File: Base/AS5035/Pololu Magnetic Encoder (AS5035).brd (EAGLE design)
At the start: 17.8 x 11.7 mm, 6 parts, among them U1 AS5035

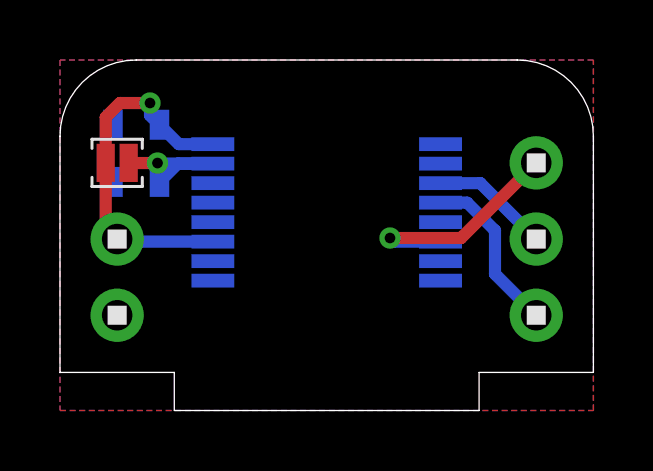
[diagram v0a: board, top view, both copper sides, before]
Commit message: CS should be tied low for QEI to work on the AS5035
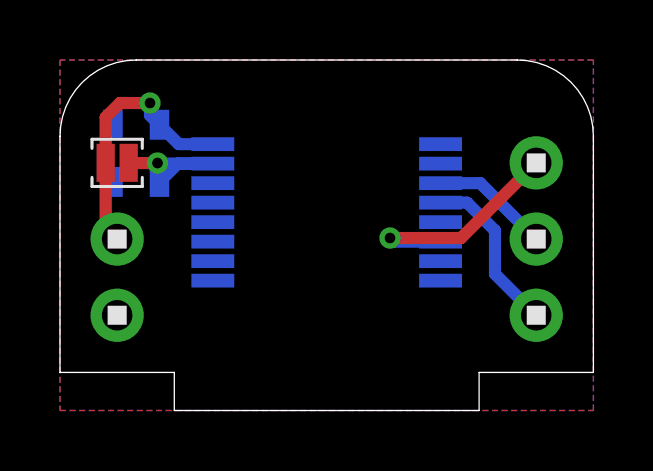
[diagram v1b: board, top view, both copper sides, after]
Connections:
- net GND: now also U1.11
- net VIN: no longer U1.11
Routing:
- net VIN: track 12.0 -> 8.91 mm
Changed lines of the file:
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@@
 <contactref element="C1" pad="1"/>
 <contactref element="J1" pad="2"/>
-<contactref element="U1" pad="11"/>
 <contactref element="U$5" pad="1"/>
 <wire x1="5.095" y1="8.879" x2="3.961" y2="8.879" width="0.4064" layer="16"/>
 <wire x1="3.961" y1="8.879" x2="3.315" y2="9.525" width="0.4064" layer="16"/>
-<wire x1="5.095" y1="5.629" x2="1.991" y2="5.629" width="0.4064" layer="16"/>
 <wire x1="1.991" y1="5.629" x2="1.905" y2="5.715" width="0.4064" layer="16"/>
 <wire x1="1.905" y1="5.715" x2="1.524" y2="6.096" width="0.4064" layer="1"/>
@@
 </polygon>
 <contactref element="U$5" pad="2"/>
+<contactref element="U1" pad="11"/>
 </signal>
 <signal name="N$4">
